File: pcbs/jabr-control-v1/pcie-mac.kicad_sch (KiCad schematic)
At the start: 37 parts, among them U5001 LAN7431_YXX

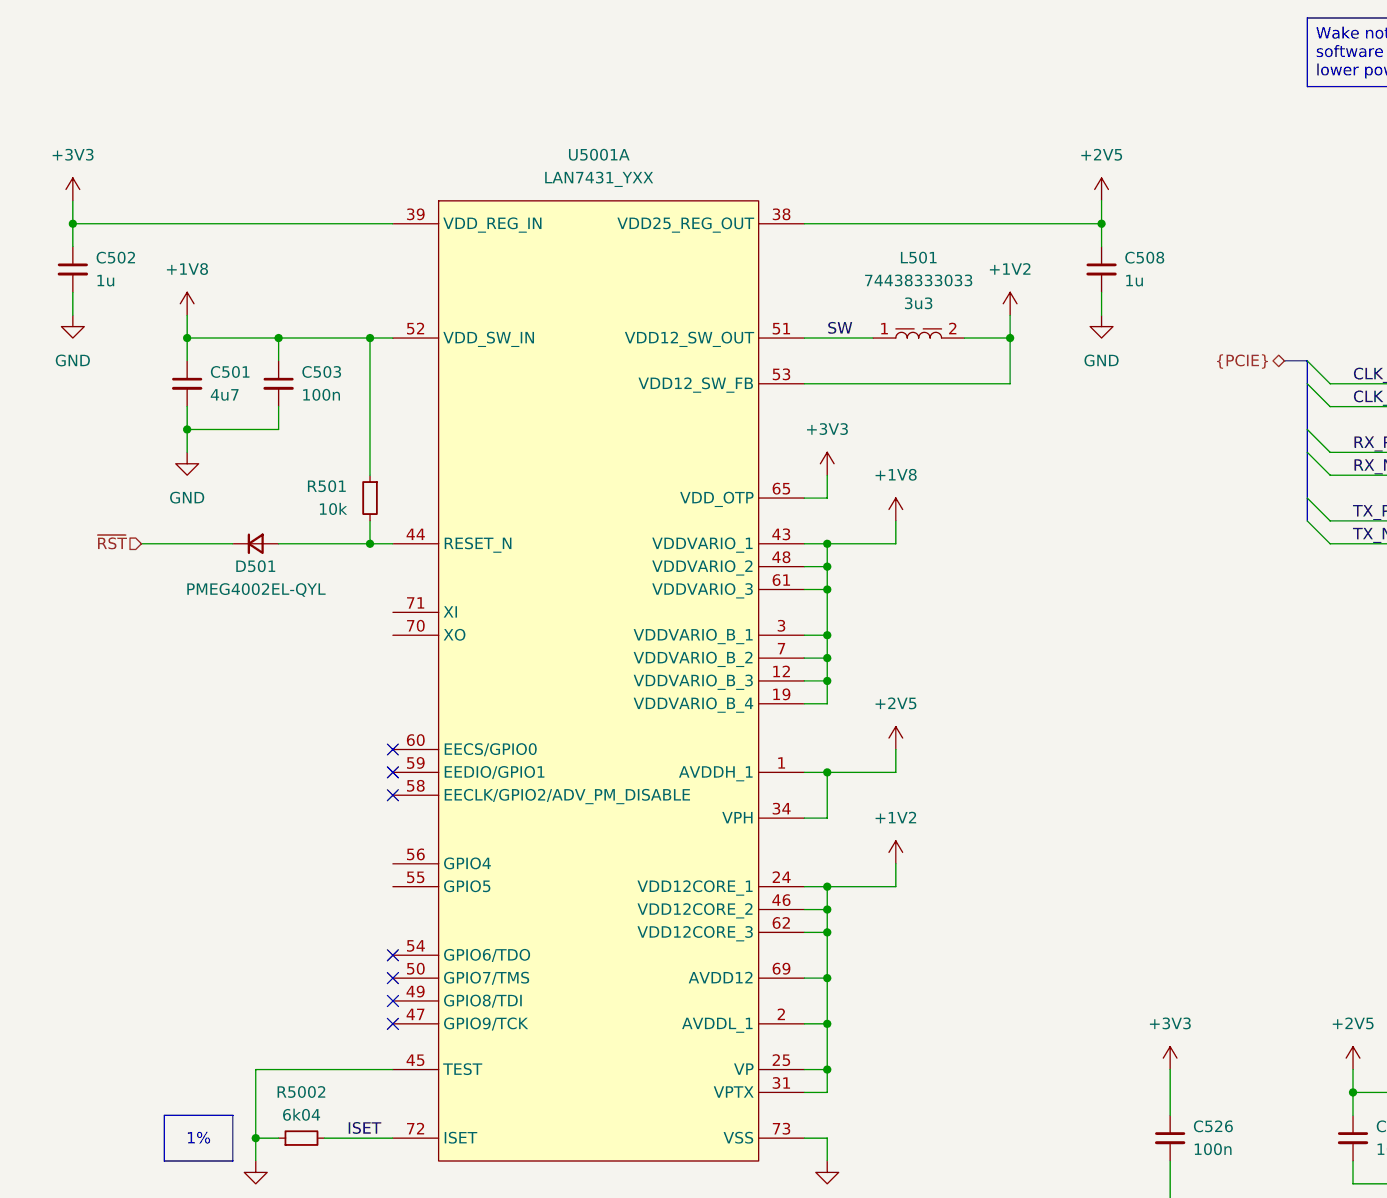
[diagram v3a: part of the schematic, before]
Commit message: Schematic nearing completion, need to do GPIO and PHY decouplings caps
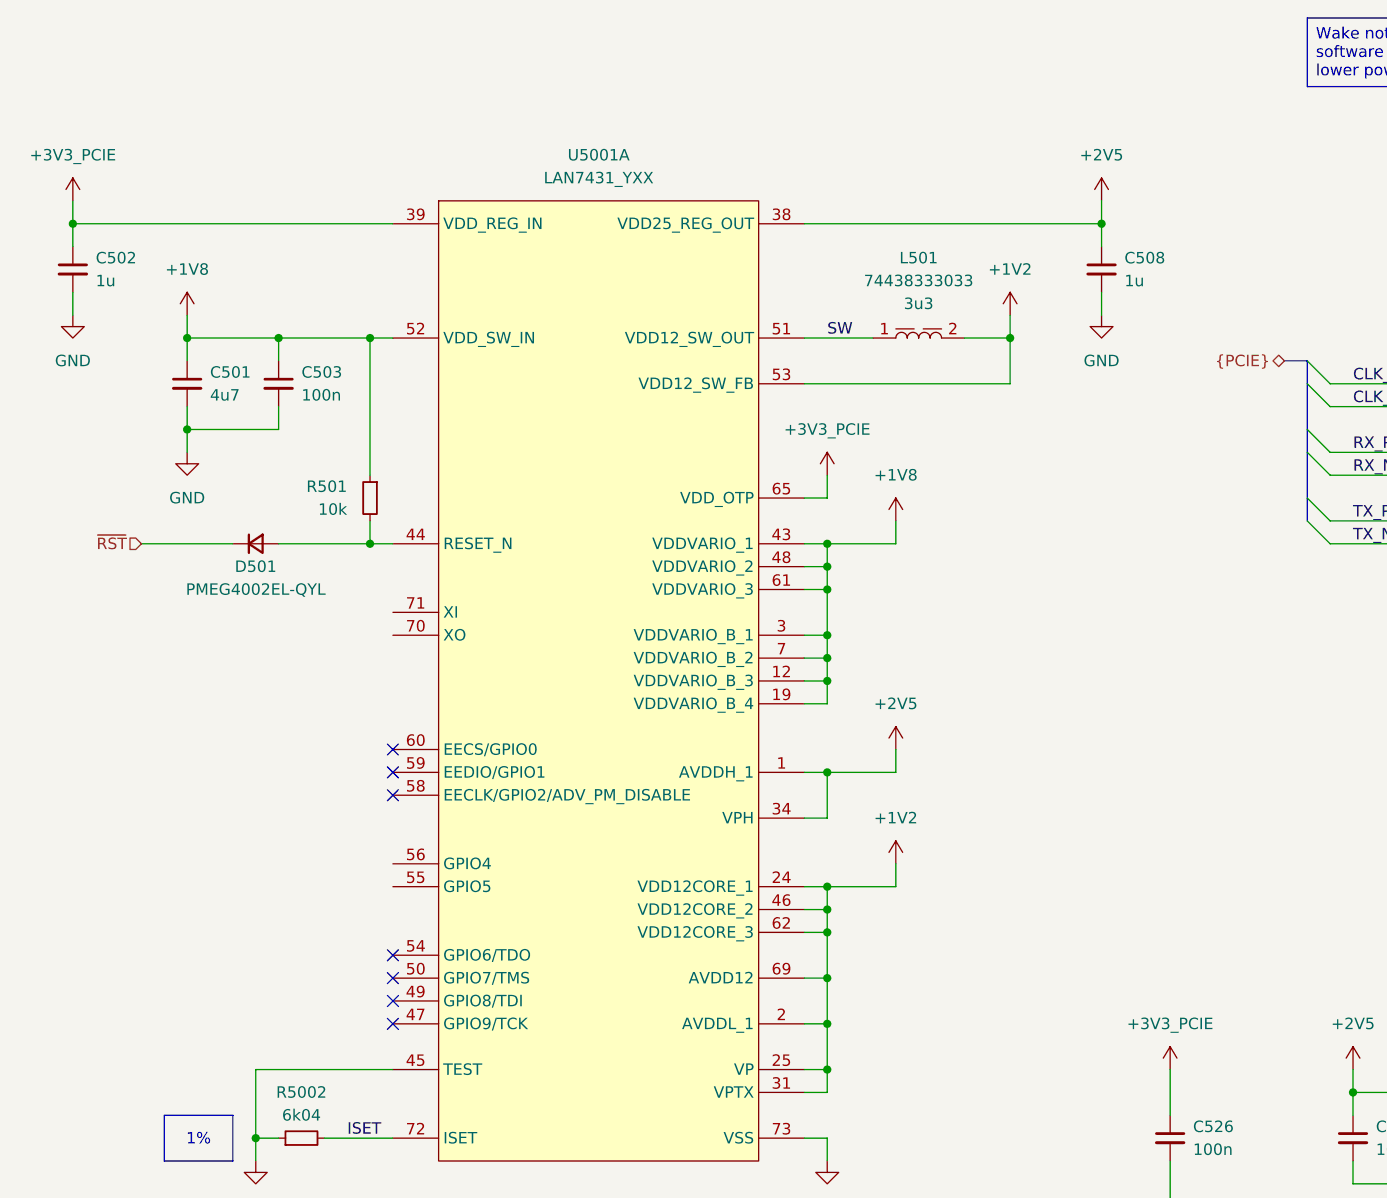
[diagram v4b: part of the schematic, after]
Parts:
- C501, C502, C503, C504, C505, C506, C507, C508, C509, C510, C511, C512, C513, C514, C515, C516, C517, C518, C519, C520, C521, C522, C523, C524, C525, C526: symbol DEV:C_SMALL_IO -> DEV:C_SMALL
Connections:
- net +3V3 renamed +3V3_PCIE
